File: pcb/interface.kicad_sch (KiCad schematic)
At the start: 40 parts, among them J4 Conn_01x24, Q1 Q_NMOS, SW1 SW_Push, SW2 SW_Push, SW3 SW_Push

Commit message: Clean up sch
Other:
- note added: "Buttons"
- note added: "RGB LEDs"
- note added: "ePaper Display"
- moved on the sheet: C15, C16, C17, C18, C19, C20, C21, C22, C23, C24, C26, C27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

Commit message: Footprints
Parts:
- C15, C16, C17, C19, C21, C22, C23, C24, C26, C27, C28, C29, C30, C31, C32, C33, C34, C35, C36, L3: footprint (none) -> Capacitor_SMD:C_0603_1608Metric
- C18, C20: footprint (none) -> Capacitor_SMD:C_0805_2012Metric
- D1, D2, D3: footprint (none) -> Diode_SMD:D_SOD-123
- J4: footprint (none) -> Connector_FFC-FPC:Amphenol_F32Q-1A7x1-11024_1x24-1MP_P0.5mm_Horizontal
- Q1: footprint (none) -> Package_TO_SOT_SMD:SC-70-8
- R3, R4: footprint (none) -> Resistor_SMD:R_0603_1608Metric
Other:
- note added: "Boost"
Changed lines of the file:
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@@
 		)
 	)
+	(text "Boost"
+		(exclude_from_sim no)
+		(at 131.572 111.506 0)
+		(effects
+			(font
+				(size 1.27 1.27)
+				(color 8 6 255 1)
+			)
+		)
+	)
 	(text "Buttons\n"
 		(exclude_from_sim no)
@@
 			)
 		)
-		(property "Footprint" ""
+		(property "Footprint" "Capacitor_SMD:C_0805_2012Metric"
 			(at 120.3452 64.77 0)
 			(effects
@@
 			)
 		)
-		(property "Footprint" ""
+		(property "Footprint" "Capacitor_SMD:C_0603_1608Metric"
 			(at 245.11 103.1748 0)
 			(effects
@@
 			)
 		)
-		(property "Footprint" ""
+		(property "Footprint" "Diode_SMD:D_SOD-123"
 			(at 138.43 40.64 0)
 			(effects
@@
 			)
 		)
-		(property "Footprint" ""
+		(property "Footprint" "Capacitor_SMD:C_0603_1608Metric"
 			(at 220.98 103.1748 0)
 			(effects
@@
 			)
 		)
-		(property "Footprint" ""
+		(property "Footprint" "Capacitor_SMD:C_0603_1608Metric"
 			(at 79.7052 100.33 0)
 			(effects
@@
 			)
 		)
-		(property "Footprint" ""
+		(property "Footprint" "Capacitor_SMD:C_0603_1608Metric"
 			(at 246.38 49.8348 0)
 			(effects
@@
 			)
 		)
-		(property "Footprint" ""
+		(property "Footprint" "Capacitor_SMD:C_0603_1608Metric"
 			(at 145.7452 68.58 0)
 			(effects
@@
 			)
 		)
-		(property "Footprint" ""
+		(property "Footprint" "Capacitor_SMD:C_0603_1608Metric"
 			(at 26.3652 100.33 0)
 			(effects
@@
 			)
 		)
-		(property "Footprint" ""
+		(property "Footprint" "Resistor_SMD:R_0603_1608Metric"
 			(at 118.872 90.17 90)
 			(effects
@@
 			)
 		)
-		(property "Footprint" ""
+		(property "Footprint" "Capacitor_SMD:C_0603_1608Metric"
 			(at 198.12 49.8348 0)
 			(effects
@@
 			)
 		)
-		(property "Footprint" ""
+		(property "Footprint" "Capacitor_SMD:C_0603_1608Metric"
 			(at 222.25 49.8348 0)
 			(effects
@@
 			)
 		)
-		(property "Footprint" ""
+		(property "Footprint" "Capacitor_SMD:C_0603_1608Metric"
 			(at 59.3852 100.33 0)
 			(effects
@@
 			)
 		)
-		(property "Footprint" ""
+		(property "Footprint" "Capacitor_SMD:C_0805_2012Metric"
 			(at 133.0452 50.8 0)
 			(effects
@@
 			)
 		)
-		(property "Footprint" ""
+		(property "Footprint" "Capacitor_SMD:C_0603_1608Metric"
 			(at 39.0652 100.33 0)
 			(effects
@@
 			)
 		)
-		(property "Footprint" ""
+		(property "Footprint" "Capacitor_SMD:C_0603_1608Metric"
 			(at 270.51 49.8348 0)
 			(effects
@@
 			)
 		)
-		(property "Footprint" ""
+		(property "Footprint" "Capacitor_SMD:C_0603_1608Metric"
 			(at 131.7752 170.18 0)
 			(effects
@@
 			)
 		)
-		(property "Footprint" ""
+		(property "Footprint" "Diode_SMD:D_SOD-123"
 			(at 138.43 31.75 0)
 			(effects
@@
 			)
 		)
-		(property "Footprint" ""
+		(property "Footprint" "Capacitor_SMD:C_0603_1608Metric"
 			(at 63.8048 43.18 0)
 			(effects
@@
 			)
 		)
-		(property "Footprint" ""
+		(property "Footprint" "Capacitor_SMD:C_0603_1608Metric"
 			(at 49.2252 100.33 0)
 			(effects
@@
 			)
 		)
-		(property "Footprint" ""
+		(property "Footprint" "Capacitor_SMD:C_0603_1608Metric"
 			(at 93.6752 170.18 0)
 			(effects
@@
 			)
 		)
-		(property "Footprint" ""
+		(property "Footprint" "Capacitor_SMD:C_0603_1608Metric"
 			(at 125.73 54.61 0)
 			(effects
@@
 			)
 		)
-		(property "Footprint" ""
+		(property "Footprint" "Capacitor_SMD:C_0603_1608Metric"
 			(at 56.8452 170.18 0)
 			(effects
@@
 			)
 		)
-		(property "Footprint" ""
+		(property "Footprint" "Capacitor_SMD:C_0603_1608Metric"
 			(at 69.5452 100.33 0)
 			(effects
@@
 			)
 		)
-		(property "Footprint" ""
+		(property "Footprint" "Resistor_SMD:R_0603_1608Metric"
 			(at 130.302 90.17 90)
 			(effects
@@
 			)
 		)
-		(property "Footprint" ""
+		(property "Footprint" "Connector_FFC-FPC:Amphenol_F32Q-1A7x1-11024_1x24-1MP_P0.5mm_Horizontal"
 			(at 86.36 60.96 0)
 			(effects
@@
 			)
 		)
-		(property "Footprint" ""
+		(property "Footprint" "Package_TO_SOT_SMD:SC-70-8"
 			(at 134.62 73.66 0)
 			(effects
@@
 			)
 		)
-		(property "Footprint" ""
+		(property "Footprint" "Diode_SMD:D_SOD-123"
 			(at 138.43 59.69 0)
 			(effects
@@
 			)
 		)
-		(property "Footprint" ""
+		(property "Footprint" "Capacitor_SMD:C_0603_1608Metric"
 			(at 269.24 103.1748 0)
 			(effects
@@
 			)
 		)
-		(property "Footprint" ""
+		(property "Footprint" "Capacitor_SMD:C_0603_1608Metric"
 			(at 196.85 103.1748 0)
 			(effects

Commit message: Add comment
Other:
- note added: "TODO: Change to smaller devices"
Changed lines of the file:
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@@
+		)
+	)
+	(text "TODO: Change to smaller devices"
+		(exclude_from_sim no)
+		(at 228.854 88.138 0)
+		(effects
+			(font
+				(size 2.032 2.032)
+				(thickness 0.4064)
+				(bold yes)
+				(color 255 0 255 1)
+			)
 		)
 	)

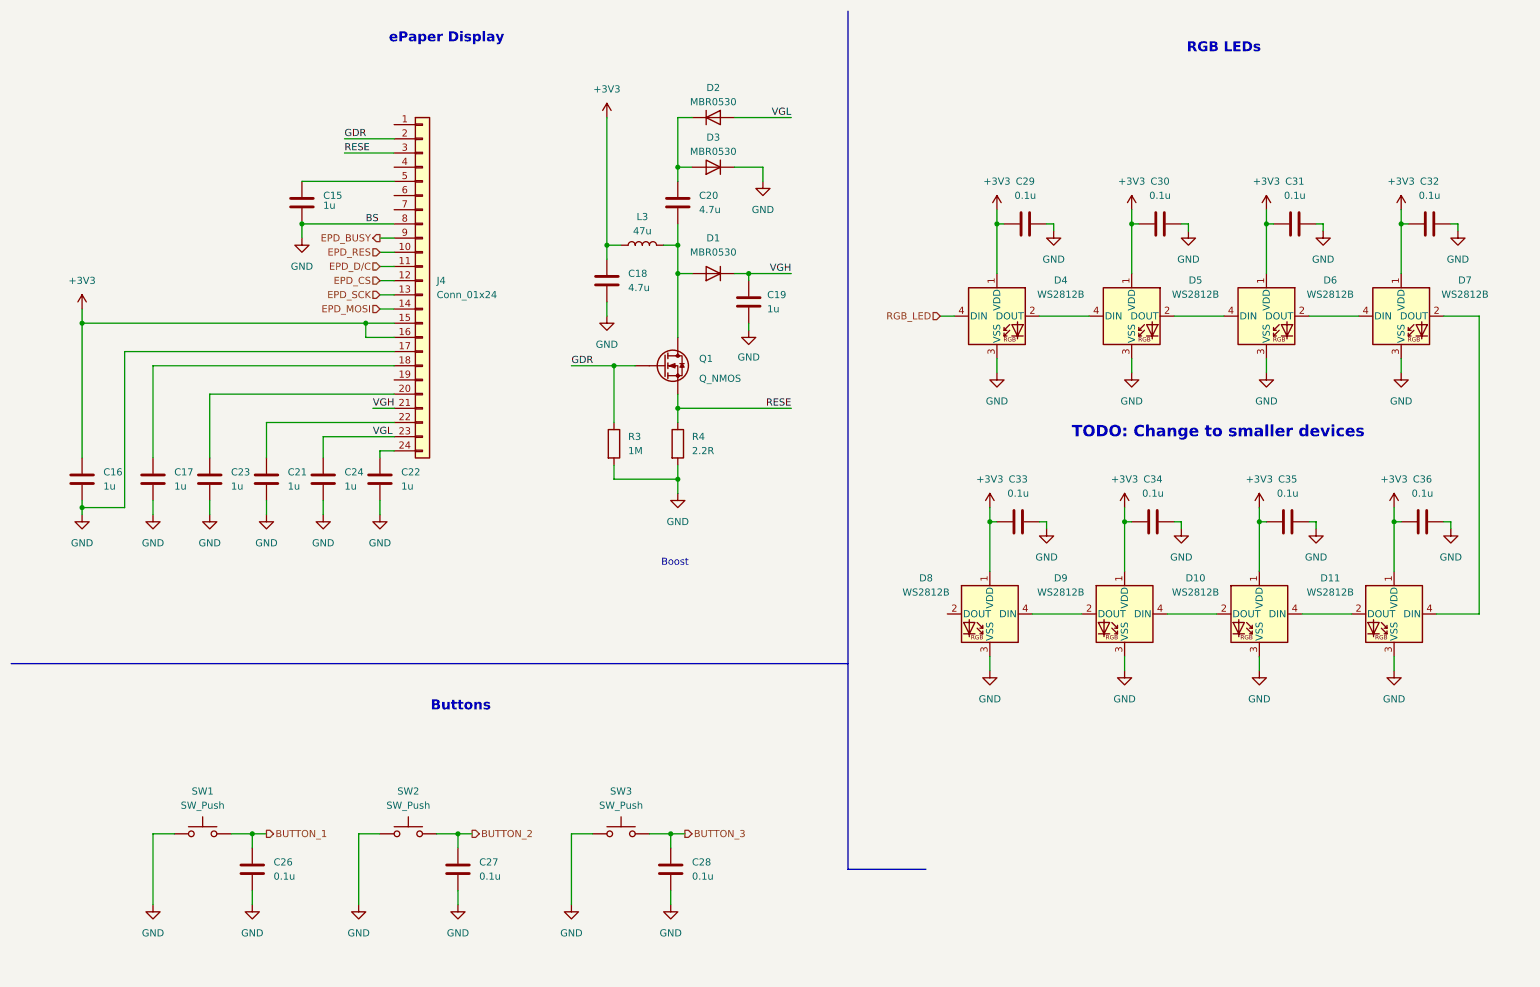
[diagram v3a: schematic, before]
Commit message: Add netclasses and usb-to-uart
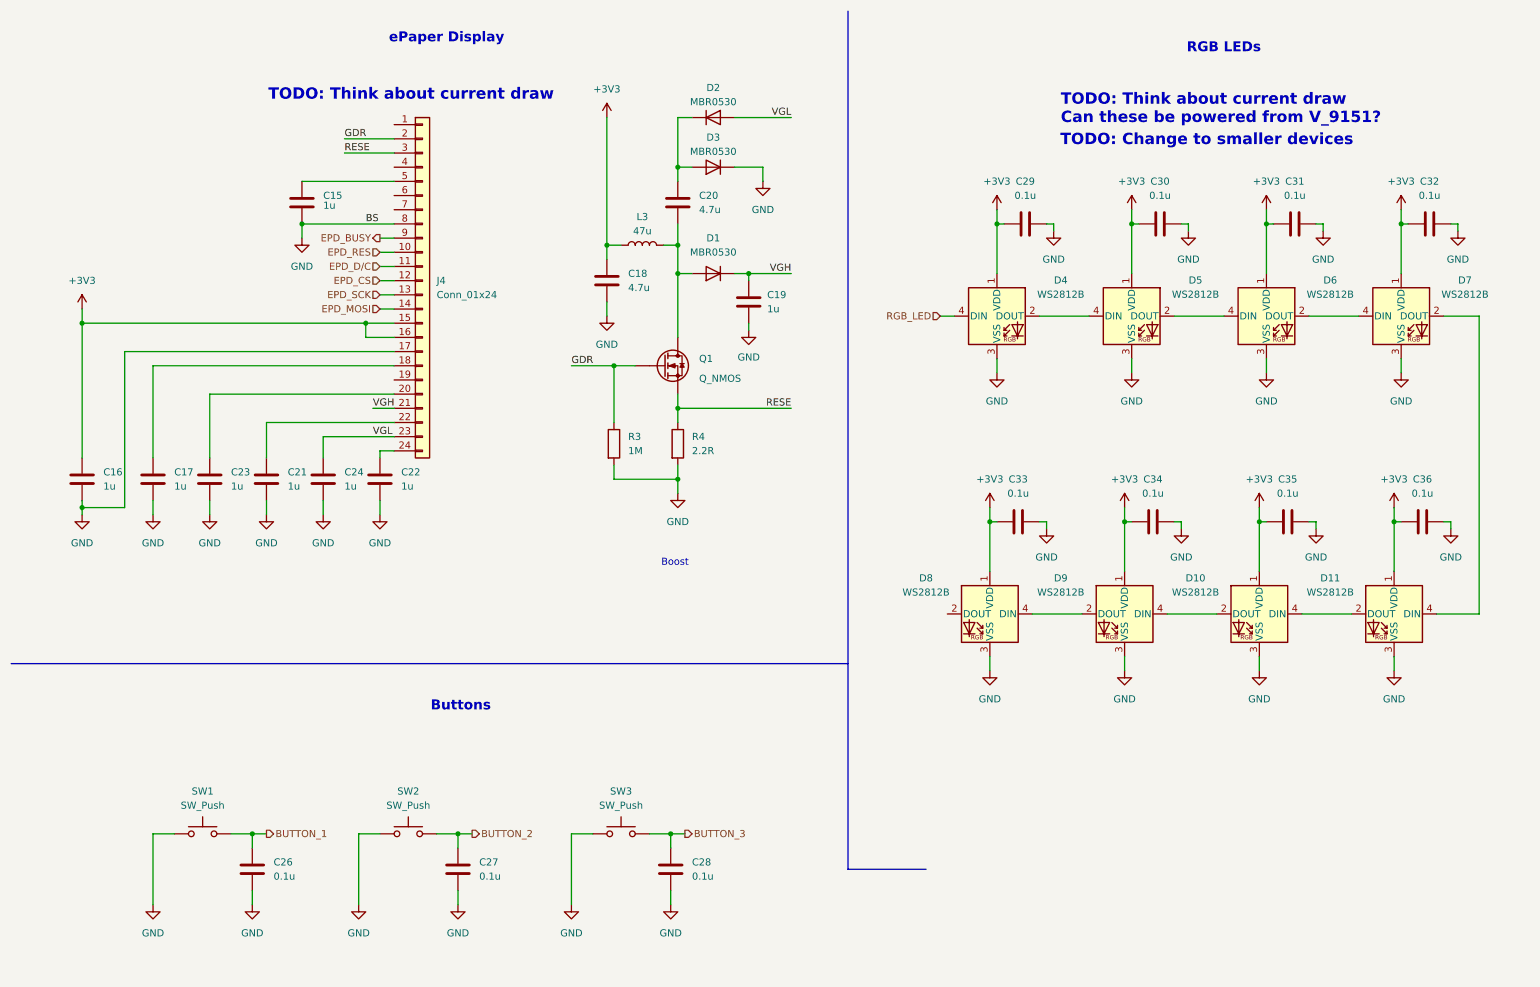
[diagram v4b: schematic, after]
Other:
- note added: "TODO: Think about current draw"
- note added: "TODO: Think about current draw Can these be powered from V_9151?"
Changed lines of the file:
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@@
 	(text "TODO: Change to smaller devices"
 		(exclude_from_sim no)
-		(at 228.854 88.138 0)
+		(at 226.822 35.814 0)
+		(effects
+			(font
+				(size 2.032 2.032)
+				(thickness 0.4064)
+				(bold yes)
+				(color 255 0 255 1)
+			)
+		)
+	)
+	(text "TODO: Think about current draw"
+		(exclude_from_sim no)
+		(at 84.328 27.686 0)
 		(effects
 			(font
@@
 		)
 	)
+	(text "TODO: Think about current draw\nCan these be powered from V_9151?"
+		(exclude_from_sim no)
+		(at 200.66 30.226 0)
+		(effects
+			(font
+				(size 2.032 2.032)
+				(thickness 0.4064)
+				(bold yes)
+				(color 255 0 255 1)
+			)
+			(justify left)
+		)
+	)

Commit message: Fix display sch
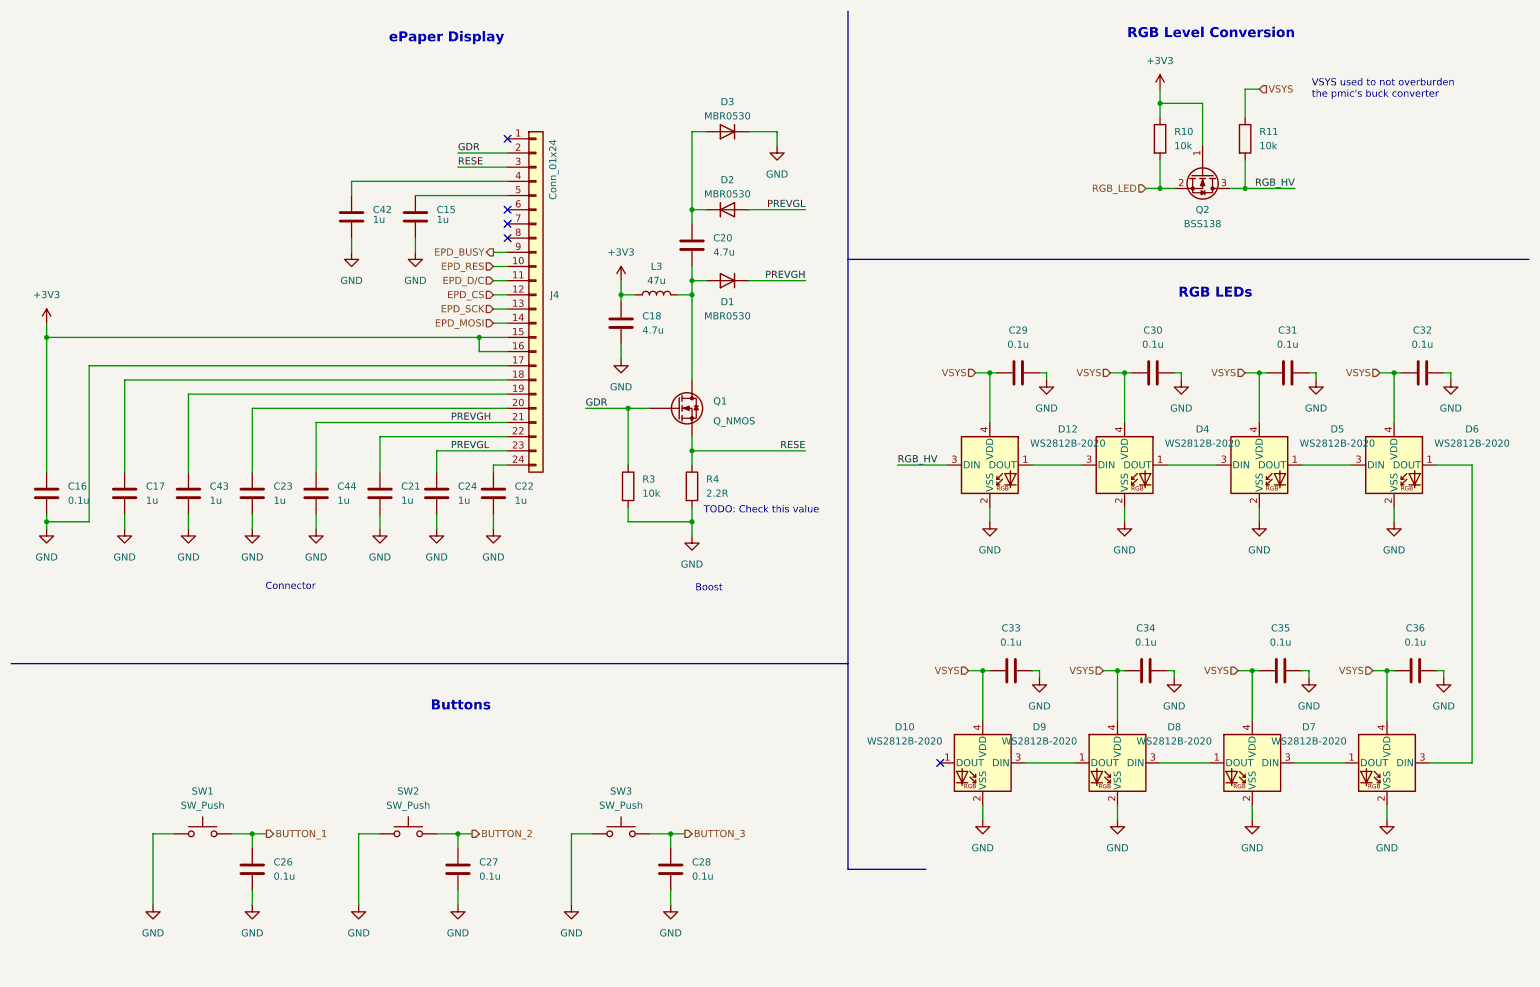
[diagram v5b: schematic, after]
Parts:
- removed C19: 1u, Capacitor_SMD:C_0603_1608Metric, symbol Device:C
- removed D10, D11, D4, D5, D6, D7, D8, D9: WS2812B, LED_SMD:LED_WS2812B_PLCC4_5.0x5.0mm_P3.2mm, symbol LED:WS2812B
- added C42, C43, C44: 1u, Capacitor_SMD:C_0603_1608Metric, symbol Device:C
- added D10, D12, D4, D5, D6, D7, D8, D9: WS2812B-2020, LED_SMD:LED_WS2812B-2020_PLCC4_2.0x2.0mm, symbol LED:WS2812B-2020
- added Q2: BSS138, Package_TO_SOT_SMD:SOT-23, symbol Transistor_FET:BSS138
- added R10, R11: 10k, symbol Device:R
- C16: value 1u -> 0.1u
- R3: value 1M -> 10k
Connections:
- net +3V3: now also Q2.1 (G), R10.1; no longer C29.1, C30.1, C31.1, C32.1, C33.1, C34.1, C35.1, C36.1
- net GND: now also C42.1, C43.2, C44.2, D10.2 (VSS), D12.2 (VSS), D4.2 (VSS), D5.2 (VSS), D6.2 (VSS), D7.2 (VSS), D8.2 (VSS), D9.2 (VSS); no longer J4.8 (Pin_8)
- net RGB_LED: now also Q2.2 (S), R10.2
- net at J4.19 (Pin_19): now also C43.1
- net at J4.4 (Pin_4): now also C42.2
- net VGH renamed PREVGH
- net PREVGH: now also C44.1
- net VGL renamed PREVGL
- new net: D5.1 (DOUT), D6.3 (DIN)
- new net: D4.1 (DOUT), D5.3 (DIN)
- new net: D6.1 (DOUT), D7.3 (DIN)
- new net: D12.1 (DOUT), D4.3 (DIN)
- new net: D7.1 (DOUT), D8.3 (DIN)
- new net: D10.3 (DIN), D9.1 (DOUT)
- new net: D8.1 (DOUT), D9.3 (DIN)
- new net RGB_HV: D12.3 (DIN), Q2.3 (D), R11.2
- new net VSYS: C29.1, C30.1, C31.1, C32.1, C33.1, C34.1, C35.1, C36.1, D10.4 (VDD), D12.4 (VDD), D4.4 (VDD), D5.4 (VDD), D6.4 (VDD), D7.4 (VDD), D8.4 (VDD), D9.4 (VDD), R11.1
- no-connect marks 0 -> 5
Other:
- note added: "Connector"
- note added: "RGB Level Conversion"
- note added: "TODO: Check this value"
- note added: "VSYS used to not overburden the pmic's buck converter"
- note removed: "TODO: Change to smaller devices"
- note removed: "TODO: Think about current draw"
- note removed: "TODO: Think about current draw Can these be powered from V_9151?"
- moved on the sheet: C15, C16, C17, C18, C20, C21, C22, C23, C24, C29, C30, C31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

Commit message: clean up
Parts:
- R10, R11: footprint (none) -> Resistor_SMD:R_0603_1608Metric
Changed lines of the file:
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@@
 			)
 		)
-		(property "Footprint" ""
+		(property "Footprint" "Resistor_SMD:R_0603_1608Metric"
 			(at 231.902 35.56 90)
 			(effects
@@
 			)
 		)
-		(property "Footprint" ""
+		(property "Footprint" "Resistor_SMD:R_0603_1608Metric"
 			(at 216.662 35.56 90)
 			(effects

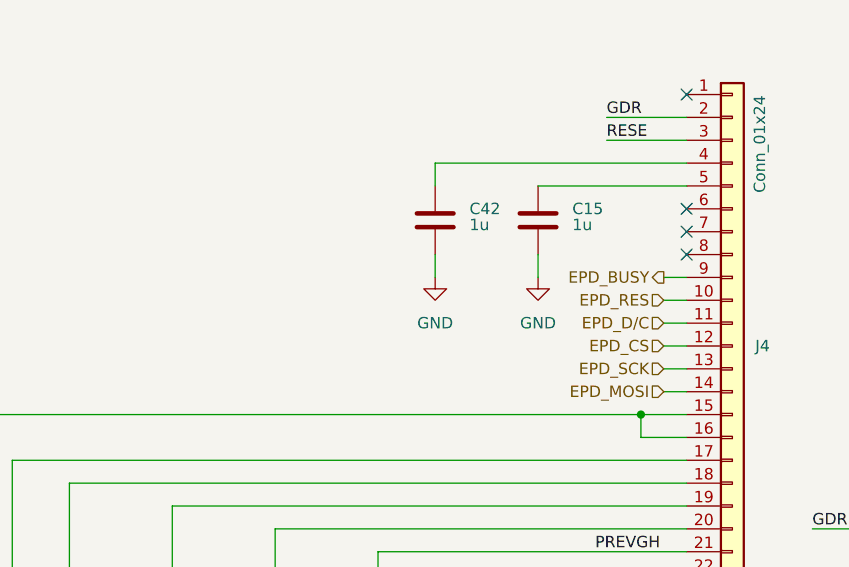
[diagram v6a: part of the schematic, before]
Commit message: Bus for epaper
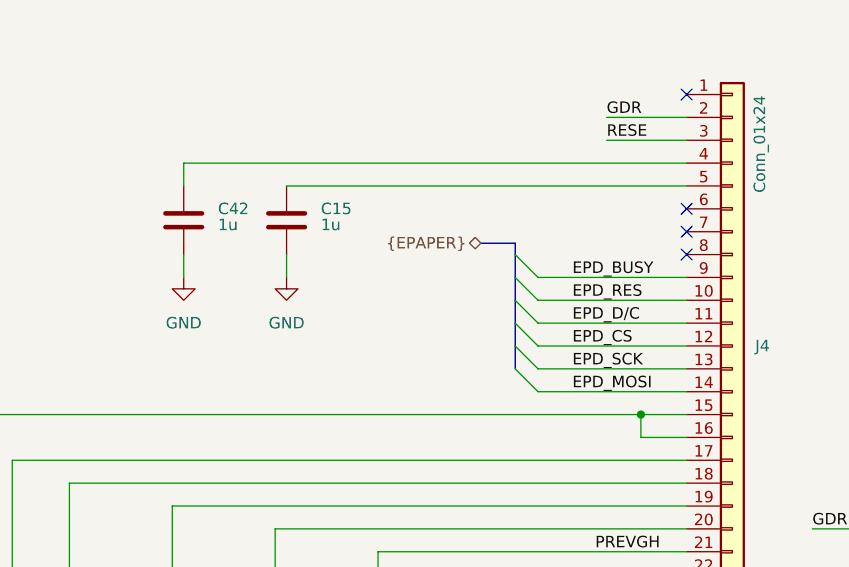
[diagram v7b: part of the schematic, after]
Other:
- moved on the sheet: C15, C42
